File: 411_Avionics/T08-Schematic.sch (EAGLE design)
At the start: 50 parts, among them IC1 BQ24022, J1 USB-MICROB, J3 JST-PH-2-SMT-RA, U1 LP5907, U2 M25P10-AVMN6TP_TR, U3 LSM9DS0, U5 LTC1998, U6 ATMEGA32U4-AU, X1 8MHz

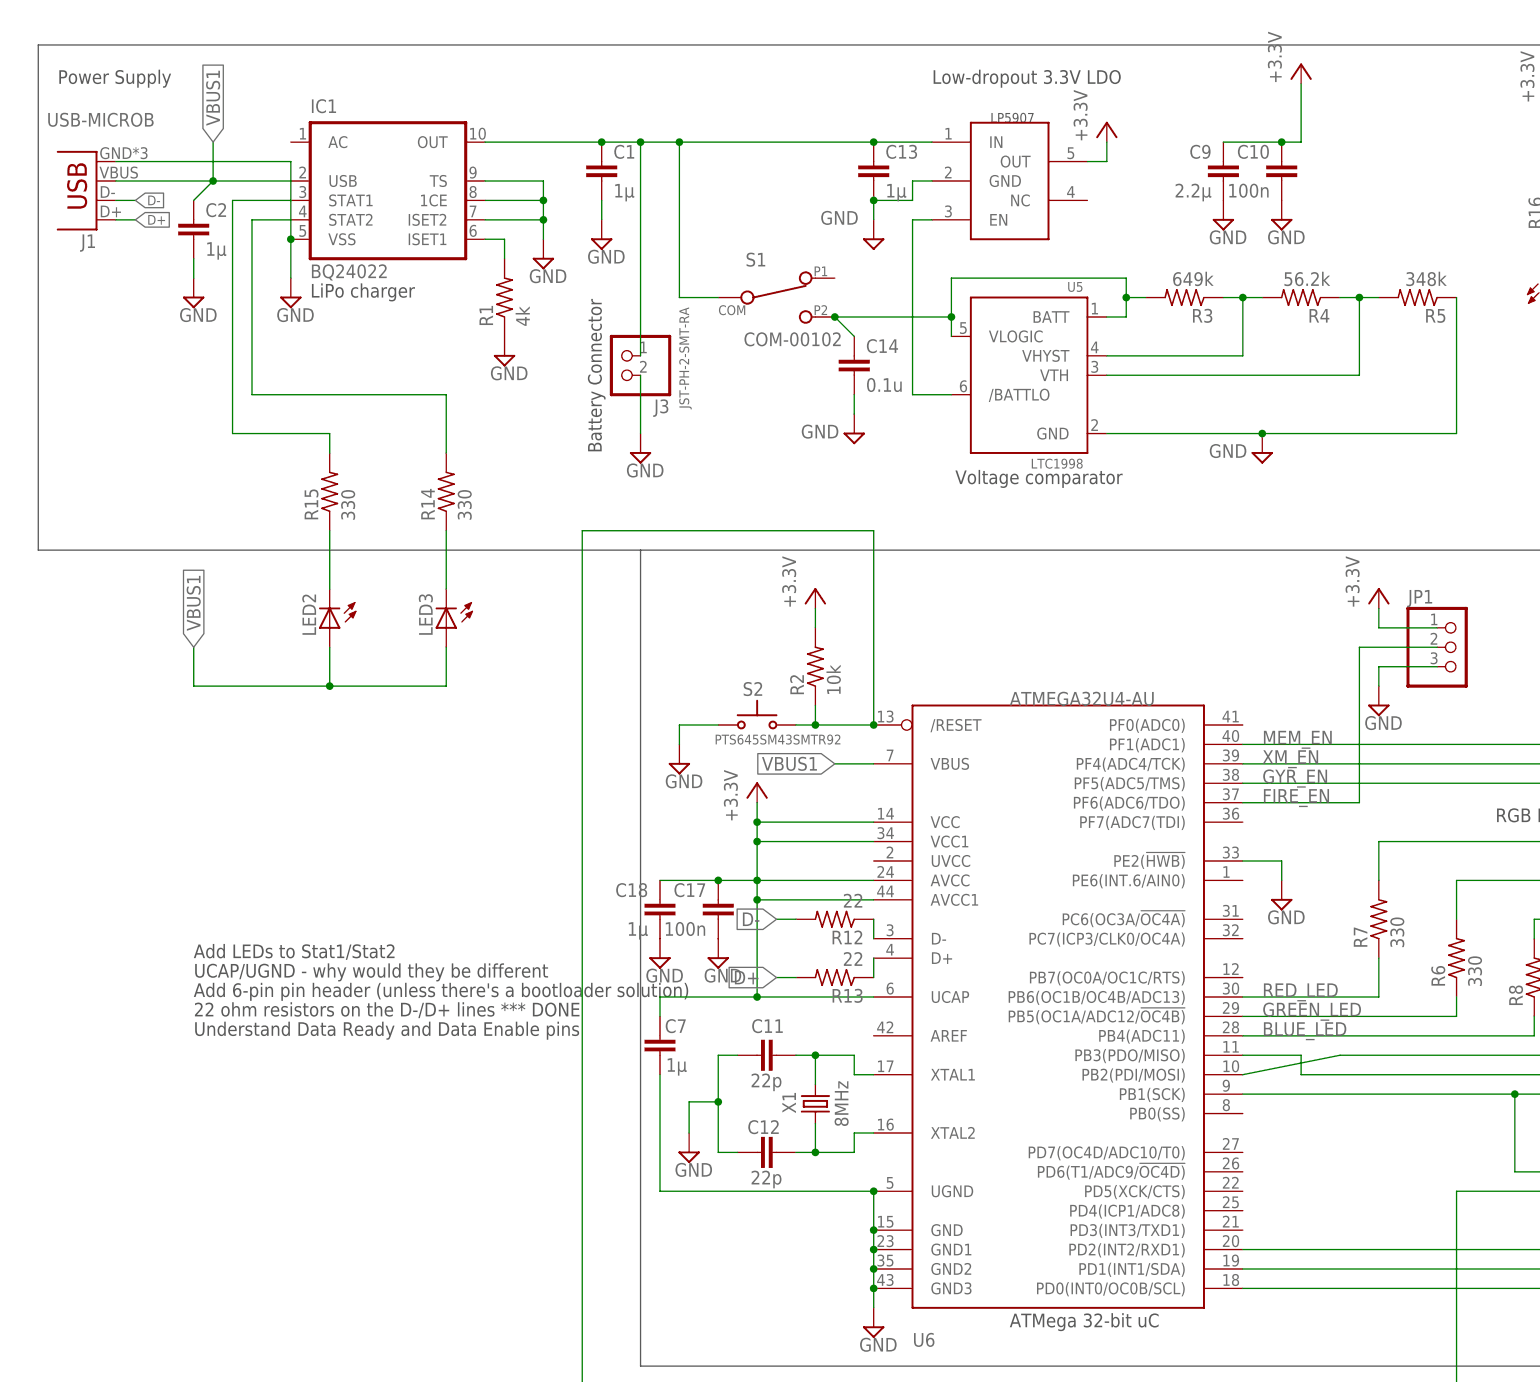
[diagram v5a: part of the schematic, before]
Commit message: Added 0 ohm resistor to #HWB line. Added test points to unpopulated GPIO.
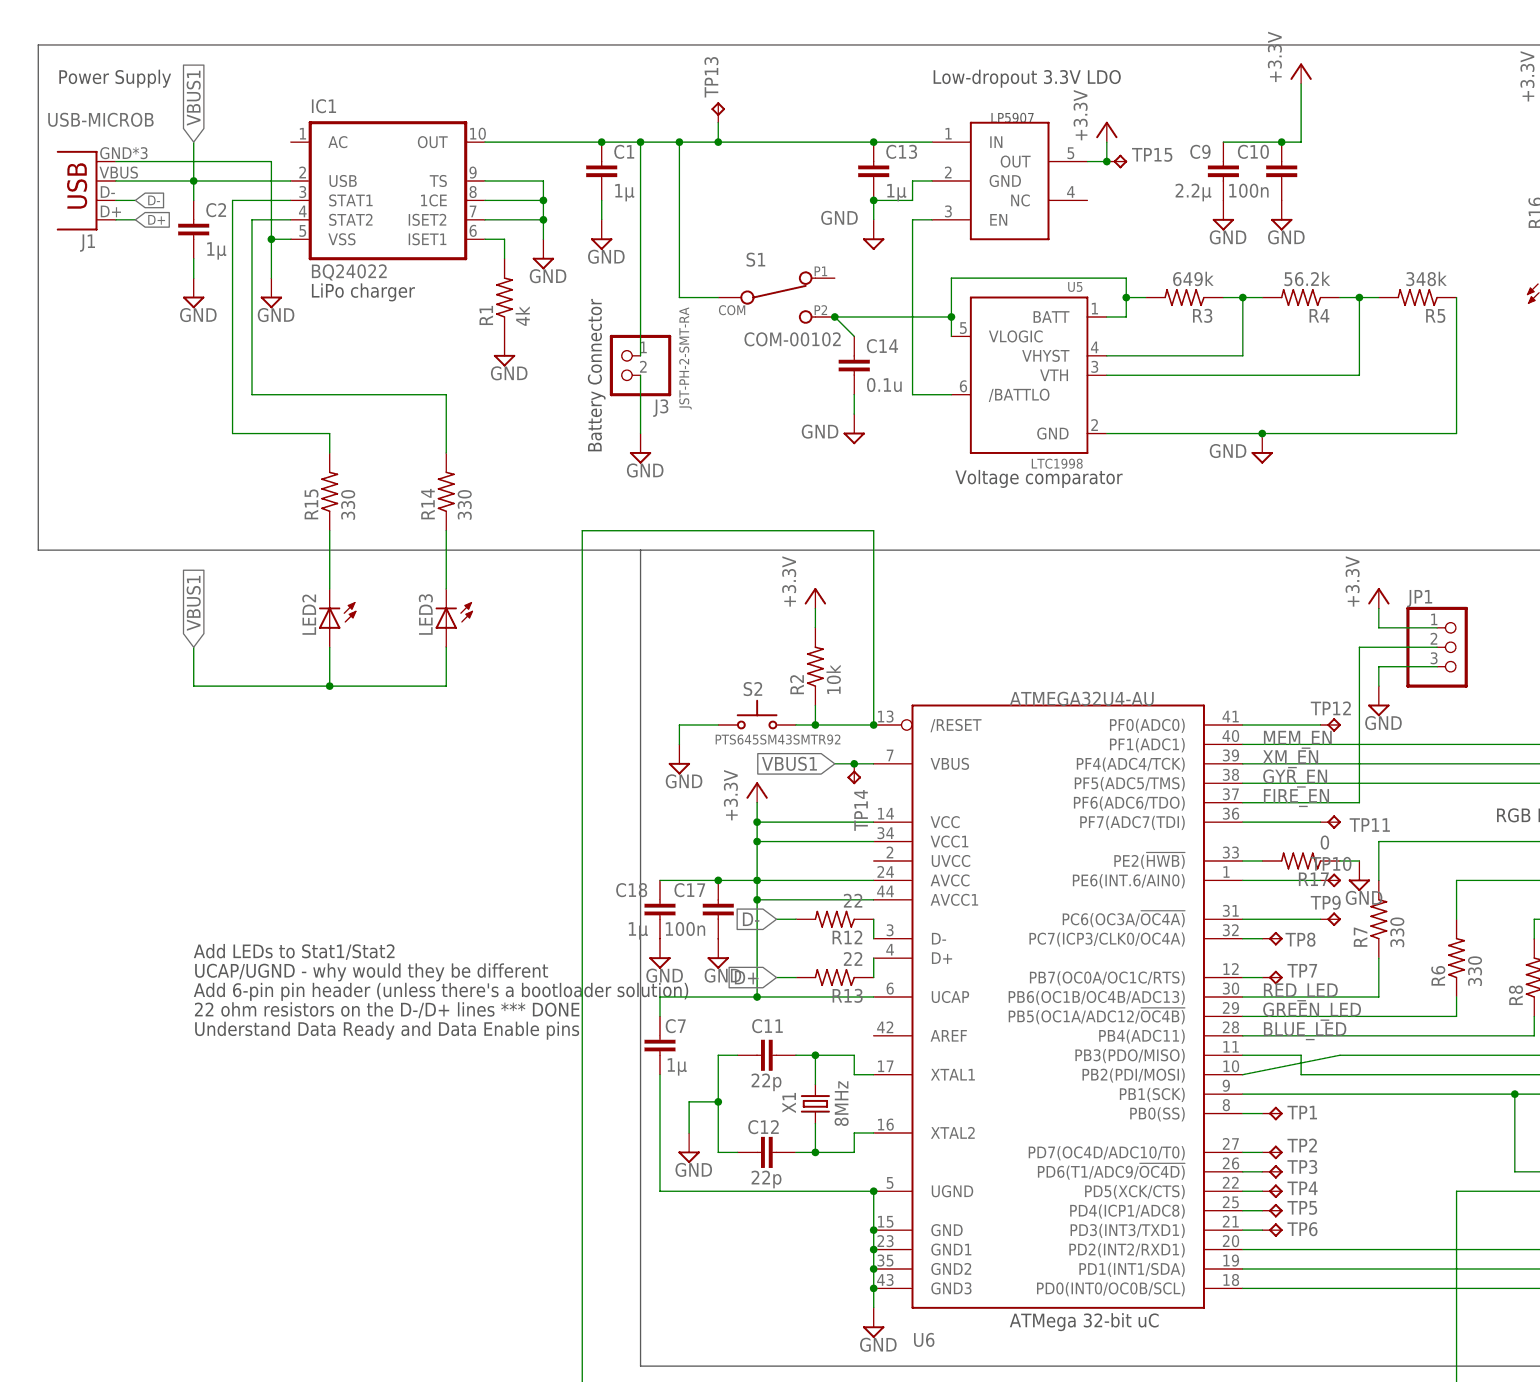
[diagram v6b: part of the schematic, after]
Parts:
- added R17: 0, rcl:R-US_R0603
- added TP1, TP10, TP11, TP12, TP13, TP14, TP15, TP2, TP3, TP4, TP5, TP6, TP7, TP8, TP9: TPTP08R, testpad:TPTP08R
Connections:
- new net N$52: TP3.TP, U6.PD6(T1/ADC9/!OC4D)
- new net N$54: TP12.TP, U6.PF0(ADC0)
- new net N$55: TP11.TP, U6.PF7(ADC7(TDI)
- new net N$56: TP10.TP, U6.PE6(INT.6/AIN0)
- new net N$57: TP9.TP, U6.PC6(OC3A/!OC4A)
- new net N$58: TP8.TP, U6.PC7(ICP3/CLK0/OC4A)
- new net N$59: TP7.TP, U6.PB7(OC0A/OC1C/RTS)
- new net N$60: TP1.TP, U6.PB0(SS)
- new net N$61: TP2.TP, U6.PD7(OC4D/ADC10/T0)
- new net N$62: TP4.TP, U6.PD5(XCK/CTS)
- new net N$63: TP5.TP, U6.PD4(ICP1/ADC8)
- new net N$64: TP6.TP, U6.PD3(INT3/TXD1)
- new net N$65: R17.2, U6.PE2(!HWB)
- net GND: now also R17.1; no longer U6.PE2(!HWB)
- net N$13: now also TP13.TP
- net VBUS1: now also TP14.TP
- net VCC: now also TP15.TP

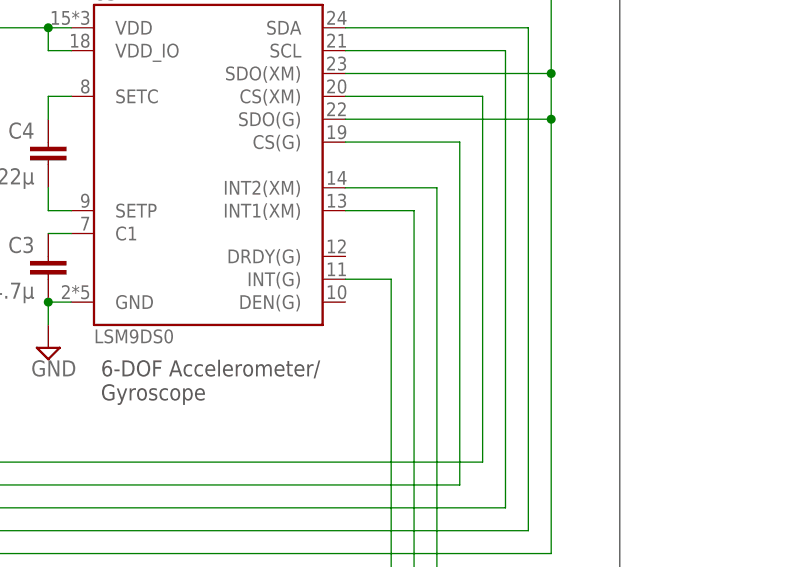
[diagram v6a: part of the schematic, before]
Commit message: Added test points to accelerometer DRDY and DENB
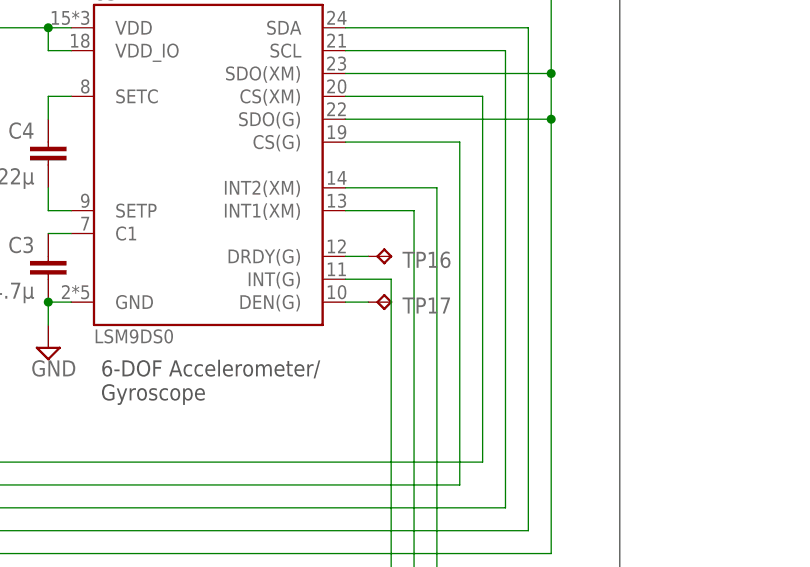
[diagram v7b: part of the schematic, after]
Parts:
- added TP16, TP17: TPTP08R, testpad:TPTP08R
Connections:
- new net N$66: TP17.TP, U3.DEN(G)
- new net N$67: TP16.TP, U3.DRDY(G)
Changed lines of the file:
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@@
 <part name="TP15" library="testpad" deviceset="TP" device="TP08R"/>
 <part name="R17" library="rcl" deviceset="R-US_" device="R0603" value="0"/>
+<part name="TP16" library="testpad" deviceset="TP" device="TP08R"/>
+<part name="TP17" library="testpad" deviceset="TP" device="TP08R"/>
 </parts>
 <sheets>
@@
 </instance>
 <instance part="R17" gate="G$1" x="182.88" y="157.48" rot="R180"/>
+<instance part="TP16" gate="G$1" x="332.74" y="162.56" smashed="yes" rot="R270">
+<attribute name="NAME" x="334.01" y="161.29" size="1.778" layer="95"/>
+<attribute name="TP_SIGNAL_NAME" x="331.47" y="161.29" size="1.778" layer="97" rot="R270"/>
+</instance>
+<instance part="TP17" gate="G$1" x="332.74" y="157.48" smashed="yes" rot="R270">
+<attribute name="NAME" x="334.01" y="156.21" size="1.778" layer="95"/>
+<attribute name="TP_SIGNAL_NAME" x="331.47" y="156.21" size="1.778" layer="97" rot="R270"/>
+</instance>
 </instances>
 <busses>
@@
 </segment>
 </net>
+<net name="N$66" class="0">
+<segment>
+<pinref part="U3" gate="G$1" pin="DEN(G)"/>
+<pinref part="TP17" gate="G$1" pin="TP"/>
+<wire x1="327.66" y1="157.48" x2="330.2" y2="157.48" width="0.1524" layer="91"/>
+</segment>
+</net>
+<net name="N$67" class="0">
+<segment>
+<pinref part="TP16" gate="G$1" pin="TP"/>
+<pinref part="U3" gate="G$1" pin="DRDY(G)"/>
+<wire x1="330.2" y1="162.56" x2="327.66" y2="162.56" width="0.1524" layer="91"/>
+</segment>
+</net>
